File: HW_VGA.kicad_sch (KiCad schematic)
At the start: 3 parts, among them U1 25.175 MHz, U301 GAL22V10

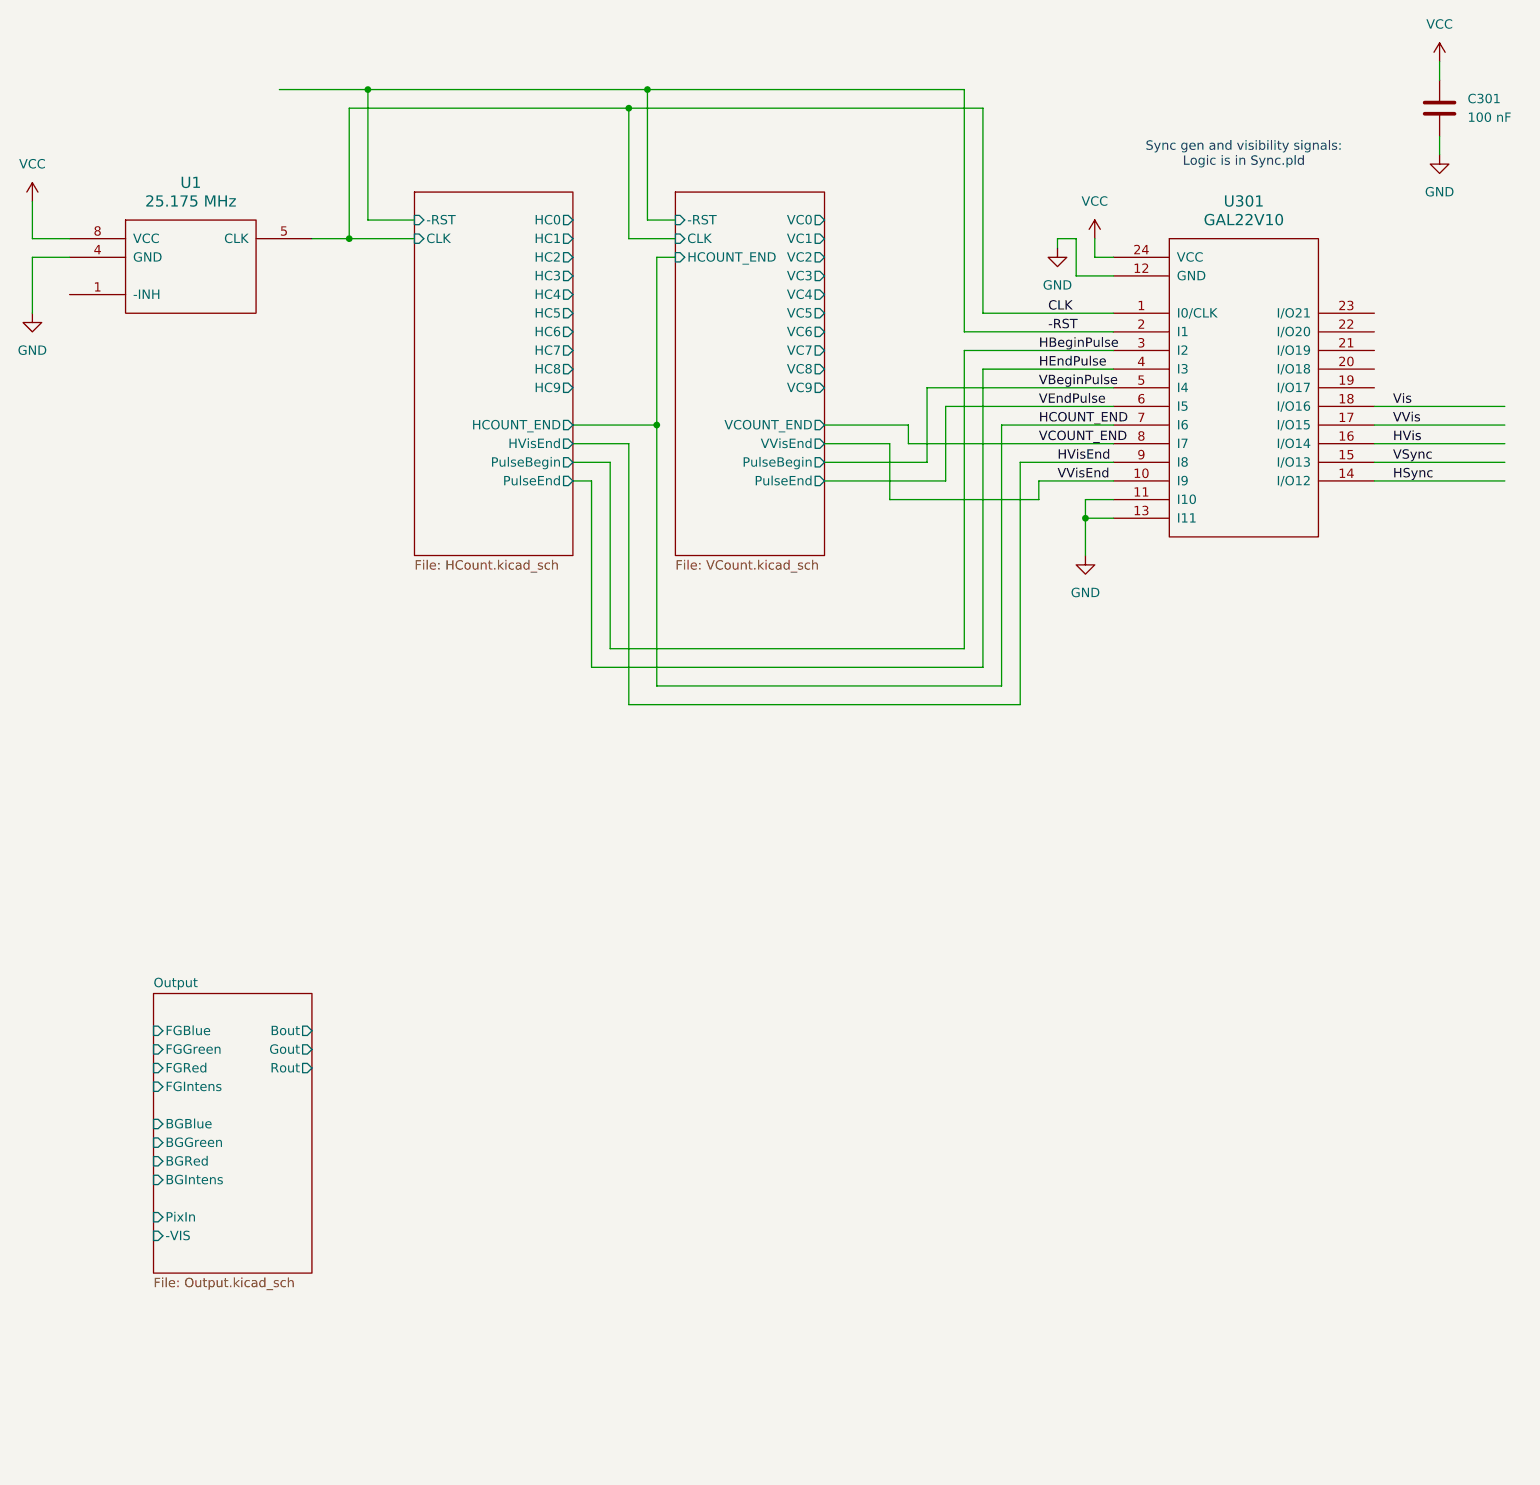
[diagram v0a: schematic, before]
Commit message: VRAM read address module
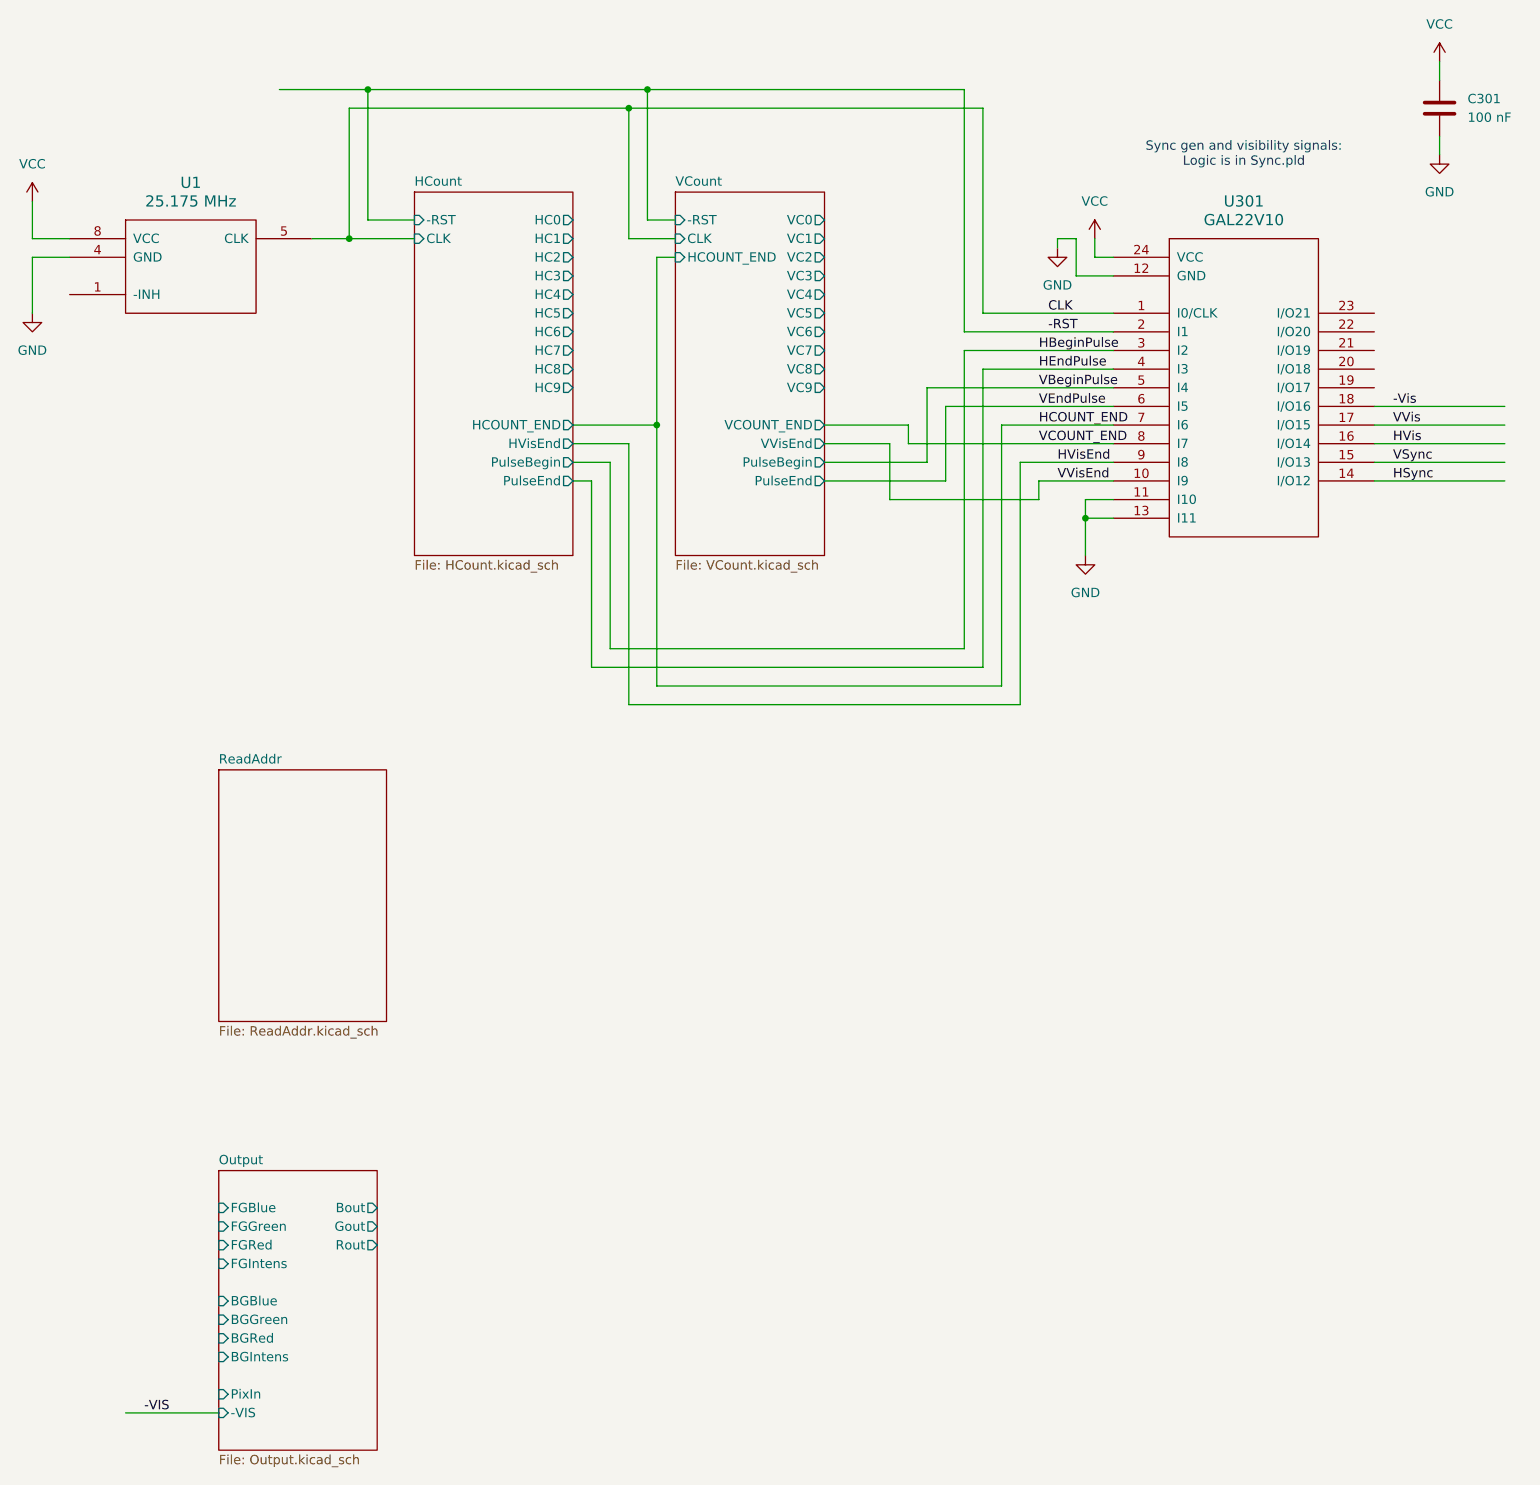
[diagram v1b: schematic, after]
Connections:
- net Vis renamed -Vis
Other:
- added sheet ReadAddr (ReadAddr.kicad_sch)
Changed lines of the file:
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@@
 	(generator "eeschema")
 	(generator_version "8.0")
-	(paper "USLetter")
+	(paper "User" 419.1 323.85)
 	(title_block
 		(title "Hardware VGA")
@@
 		(pts
 			(xy 165.1 83.82) (xy 168.91 83.82)
+		)
+		(stroke
+			(width 0)
+			(type default)
+		)
+	)
+	(wire
+		(pts
+			(xy 34.29 205.74) (xy 46.99 205.74)
 		)
 		(stroke
@@
 		)
 	)
-	(label "VSync"
-		(at 207.01 76.2 0)
+	(label "-VIS"
+		(at 36.83 205.74 0)
 		(fields_autoplaced yes)
 		(effects
@@
 		)
 	)
-	(label "VCOUNT_END"
-		(at 158.75 73.66 0)
+	(label "VSync"
+		(at 207.01 76.2 0)
 		(fields_autoplaced yes)
 		(effects
@@
 		)
 	)
-	(label "VVis"
-		(at 207.01 71.12 0)
+	(label "VCOUNT_END"
+		(at 158.75 73.66 0)
 		(fields_autoplaced yes)
 		(effects
@@
 		)
 	)
-	(label "VEndPulse"
-		(at 158.75 68.58 0)
+	(label "VVis"
+		(at 207.01 71.12 0)
 		(fields_autoplaced yes)
 		(effects
@@
 		)
 	)
-	(label "Vis"
+	(label "VEndPulse"
+		(at 158.75 68.58 0)
+		(fields_autoplaced yes)
+		(effects
+			(font
+				(size 1.27 1.27)
+			)
+			(justify left bottom)
+		)
+	)
+	(label "-Vis"
 		(at 207.01 68.58 0)
 		(fields_autoplaced yes)
@@
 				)
 				(justify left bottom)
-				(hide yes)
 			)
 		)
@@
 	)
 	(sheet
-		(at 38.1 148.59)
+		(at 46.99 172.72)
 		(size 21.59 38.1)
 		(fields_autoplaced yes)
@@
 		)
 		(property "Sheetname" "Output"
-			(at 38.1 147.8784 0)
+			(at 46.99 172.0084 0)
 			(effects
 				(font
@@
 		)
 		(property "Sheetfile" "Output.kicad_sch"
-			(at 38.1 187.2746 0)
+			(at 46.99 211.4046 0)
 			(effects
 				(font
@@
 		)
 		(pin "FGGreen" input
-			(at 38.1 156.21 180)
+			(at 46.99 180.34 180)
 			(effects
 				(font
@@
 		)
 		(pin "FGIntens" input
-			(at 38.1 161.29 180)
+			(at 46.99 185.42 180)
 			(effects
 				(font
@@
 		)
 		(pin "FGBlue" input
-			(at 38.1 153.67 180)
+			(at 46.99 177.8 180)
 			(effects
 				(font
@@
 		)
 		(pin "FGRed" input
-			(at 38.1 158.75 180)
+			(at 46.99 182.88 180)
 			(effects
 				(font
@@
 		)
 		(pin "PixIn" input
-			(at 38.1 179.07 180)
+			(at 46.99 203.2 180)
 			(effects
 				(font
@@
 		)
 		(pin "-VIS" input
-			(at 38.1 181.61 180)
+			(at 46.99 205.74 180)
 			(effects
 				(font
@@
 		)
 		(pin "BGRed" input
-			(at 38.1 171.45 180)
+			(at 46.99 195.58 180)
 			(effects
 				(font
@@
 		)
 		(pin "BGBlue" input
-			(at 38.1 166.37 180)
+			(at 46.99 190.5 180)
 			(effects
 				(font
@@
 		)
 		(pin "BGIntens" input
-			(at 38.1 173.99 180)
+			(at 46.99 198.12 180)
 			(effects
 				(font
@@
 		)
 		(pin "BGGreen" input
-			(at 38.1 168.91 180)
+			(at 46.99 193.04 180)
 			(effects
 				(font
@@
 		)
 		(pin "Bout" output
-			(at 59.69 153.67 0)
+			(at 68.58 177.8 0)
 			(effects
 				(font
@@
 		)
 		(pin "Gout" output
-			(at 59.69 156.21 0)
+			(at 68.58 180.34 0)
 			(effects
 				(font
@@
 		)
 		(pin "Rout" output
-			(at 59.69 158.75 0)
+			(at 68.58 182.88 0)
 			(effects
 				(font
@@
 	)
 	(sheet
+		(at 46.99 118.11)
+		(size 22.86 34.29)
+		(fields_autoplaced yes)
+		(stroke
+			(width 0.1524)
+			(type solid)
+		)
+		(fill
+			(color 0 0 0 0.0000)
+		)
+		(property "Sheetname" "ReadAddr"
+			(at 46.99 117.3984 0)
+			(effects
+				(font
+					(size 1.27 1.27)
+				)
+				(justify left bottom)
+			)
+		)
+		(property "Sheetfile" "ReadAddr.kicad_sch"
+			(at 46.99 152.9846 0)
+			(effects
+				(font
+					(size 1.27 1.27)
+				)
+				(justify left top)
+			)
+		)
+		(instances
+			(project "HW_VGA"
+				(path "/c4bd4b39-993a-4195-805f-b4de6fa4aea5"
+					(page "5")
+				)
+			)
+		)
+	)
+	(sheet
 		(at 109.22 39.37)
 		(size 20.32 49.53)
@@
 				)
 				(justify left bottom)
-				(hide yes)
-			)
-		)
+			)
+		)

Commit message: sketch of pixel generation logic
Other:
- added sheet Pixgen (Pixgen.kicad_sch)
- sheet ReadAddr ports: added -CLR, CLK, CountEn, RA0, RA1, RA10, RA11, RA12, RA2, RA3, RA4, RA5, RA6, RA7, RA8, RA9; removed none
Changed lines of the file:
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@@
 	(wire
 		(pts
-			(xy 34.29 205.74) (xy 46.99 205.74)
+			(xy 80.01 205.74) (xy 92.71 205.74)
 		)
 		(stroke
@@
 	)
 	(label "-VIS"
-		(at 36.83 205.74 0)
+		(at 82.55 205.74 0)
 		(fields_autoplaced yes)
 		(effects
@@
 	)
 	(sheet
-		(at 46.99 172.72)
+		(at 92.71 172.72)
 		(size 21.59 38.1)
 		(fields_autoplaced yes)
@@
 		)
 		(property "Sheetname" "Output"
-			(at 46.99 172.0084 0)
+			(at 92.71 172.0084 0)
 			(effects
 				(font
@@
 		)
 		(property "Sheetfile" "Output.kicad_sch"
-			(at 46.99 211.4046 0)
+			(at 92.71 211.4046 0)
 			(effects
 				(font
@@
 		)
 		(pin "FGGreen" input
-			(at 46.99 180.34 180)
+			(at 92.71 180.34 180)
 			(effects
 				(font
@@
 		)
 		(pin "FGIntens" input
-			(at 46.99 185.42 180)
+			(at 92.71 185.42 180)
 			(effects
 				(font
@@
 		)
 		(pin "FGBlue" input
-			(at 46.99 177.8 180)
+			(at 92.71 177.8 180)
 			(effects
 				(font
@@
 		)
 		(pin "FGRed" input
-			(at 46.99 182.88 180)
+			(at 92.71 182.88 180)
 			(effects
 				(font
@@
 		)
 		(pin "PixIn" input
-			(at 46.99 203.2 180)
+			(at 92.71 203.2 180)
 			(effects
 				(font
@@
 		)
 		(pin "-VIS" input
-			(at 46.99 205.74 180)
+			(at 92.71 205.74 180)
 			(effects
 				(font
@@
 		)
 		(pin "BGRed" input
-			(at 46.99 195.58 180)
+			(at 92.71 195.58 180)
 			(effects
 				(font
@@
 		)
 		(pin "BGBlue" input
-			(at 46.99 190.5 180)
+			(at 92.71 190.5 180)
 			(effects
 				(font
@@
 		)
 		(pin "BGIntens" input
-			(at 46.99 198.12 180)
+			(at 92.71 198.12 180)
 			(effects
 				(font
@@
 		)
 		(pin "BGGreen" input
-			(at 46.99 193.04 180)
+			(at 92.71 193.04 180)
 			(effects
 				(font
@@
 		)
 		(pin "Bout" output
-			(at 68.58 177.8 0)
+			(at 114.3 177.8 0)
 			(effects
 				(font
@@
 		)
 		(pin "Gout" output
-			(at 68.58 180.34 0)
+			(at 114.3 180.34 0)
 			(effects
 				(font
@@
 		)
 		(pin "Rout" output
-			(at 68.58 182.88 0)
+			(at 114.3 182.88 0)
 			(effects
 				(font
@@
 	)
 	(sheet
-		(at 46.99 118.11)
-		(size 22.86 34.29)
+		(at 46.99 113.03)
+		(size 26.67 39.37)
 		(fields_autoplaced yes)
 		(stroke
@@
 		)
 		(property "Sheetname" "ReadAddr"
-			(at 46.99 117.3984 0)
+			(at 46.99 112.3184 0)
 			(effects
 				(font
@@
 				)
 				(justify left top)
+			)
+		)
+		(pin "CLK" input
+			(at 46.99 116.84 180)
+			(effects
+				(font
+					(size 1.27 1.27)
+				)
+				(justify left)
+			)
+		)
+		(pin "-CLR" input
+			(at 46.99 119.38 180)
+			(effects
+				(font
+					(size 1.27 1.27)
+				)
+				(justify left)
+			)
+		)
+		(pin "CountEn" input
+			(at 46.99 121.92 180)
+			(effects
+				(font
+					(size 1.27 1.27)
+				)
+				(justify left)
+			)
+		)
+		(pin "RA7" output
+			(at 73.66 134.62 0)
+			(effects
+				(font
+					(size 1.27 1.27)
+				)
+				(justify right)
+			)
+		)
+		(pin "RA6" output
+			(at 73.66 132.08 0)
+			(effects
+				(font
+					(size 1.27 1.27)
+				)
+				(justify right)
+			)
+		)
+		(pin "RA5" output
+			(at 73.66 129.54 0)
+			(effects
+				(font
+					(size 1.27 1.27)
+				)
+				(justify right)
+			)
+		)
+		(pin "RA0" output
+			(at 73.66 116.84 0)
+			(effects
+				(font
+					(size 1.27 1.27)
+				)
+				(justify right)
+			)
+		)
+		(pin "RA1" output
+			(at 73.66 119.38 0)
+			(effects
+				(font
+					(size 1.27 1.27)
+				)
+				(justify right)
+			)
+		)
+		(pin "RA2" output
+			(at 73.66 121.92 0)
+			(effects
+				(font
+					(size 1.27 1.27)
+				)
+				(justify right)
+			)
+		)
+		(pin "RA3" output
+			(at 73.66 124.46 0)
+			(effects
+				(font
+					(size 1.27 1.27)
+				)
+				(justify right)
+			)
+		)
+		(pin "RA4" output
+			(at 73.66 127 0)
+			(effects
+				(font
+					(size 1.27 1.27)
+				)
+				(justify right)
+			)
+		)
+		(pin "RA8" output
+			(at 73.66 137.16 0)
+			(effects
+				(font
+					(size 1.27 1.27)
+				)
+				(justify right)
+			)
+		)
+		(pin "RA9" output
+			(at 73.66 139.7 0)
+			(effects
+				(font
+					(size 1.27 1.27)
+				)
+				(justify right)
+			)
+		)
+		(pin "RA10" output
+			(at 73.66 142.24 0)
+			(effects
+				(font
+					(size 1.27 1.27)
+				)
+				(justify right)
+			)
+		)
+		(pin "RA11" output
+			(at 73.66 144.78 0)
+			(effects
+				(font
+					(size 1.27 1.27)
+				)
+				(justify right)
+			)
+		)
+		(pin "RA12" output
+			(at 73.66 147.32 0)
+			(effects
+				(font
+					(size 1.27 1.27)
+				)
+				(justify right)
 			)
 		)
@@
 				)
 			)
+		)
+	)
+	(sheet
+		(at 36.83 172.72)
+		(size 25.4 38.1)
+		(fields_autoplaced yes)
+		(stroke
+			(width 0.1524)
+			(type solid)
+		)
+		(fill
+			(color 0 0 0 0.0000)
+		)
+		(property "Sheetname" "Pixgen"
+			(at 36.83 172.0084 0)
+			(effects
+				(font
+					(size 1.27 1.27)
+				)
+				(justify left bottom)
+			)
+		)
+		(property "Sheetfile" "Pixgen.kicad_sch"
+			(at 36.83 211.4046 0)
+			(effects
+				(font
+					(size 1.27 1.27)
+				)
+				(justify left top)
+			)
+		)
+		(instances
+			(project "HW_VGA"
+				(path "/c4bd4b39-993a-4195-805f-b4de6fa4aea5"
+					(page "6")
+				)
+			)
